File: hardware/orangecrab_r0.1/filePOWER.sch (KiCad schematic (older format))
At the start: 48 parts, among them J5 JST, U1 FAN53541, U10 NCP115-2.5, U2 FAN53541, U5 BQ24232, U7 FAN53541, U8 TPS51206

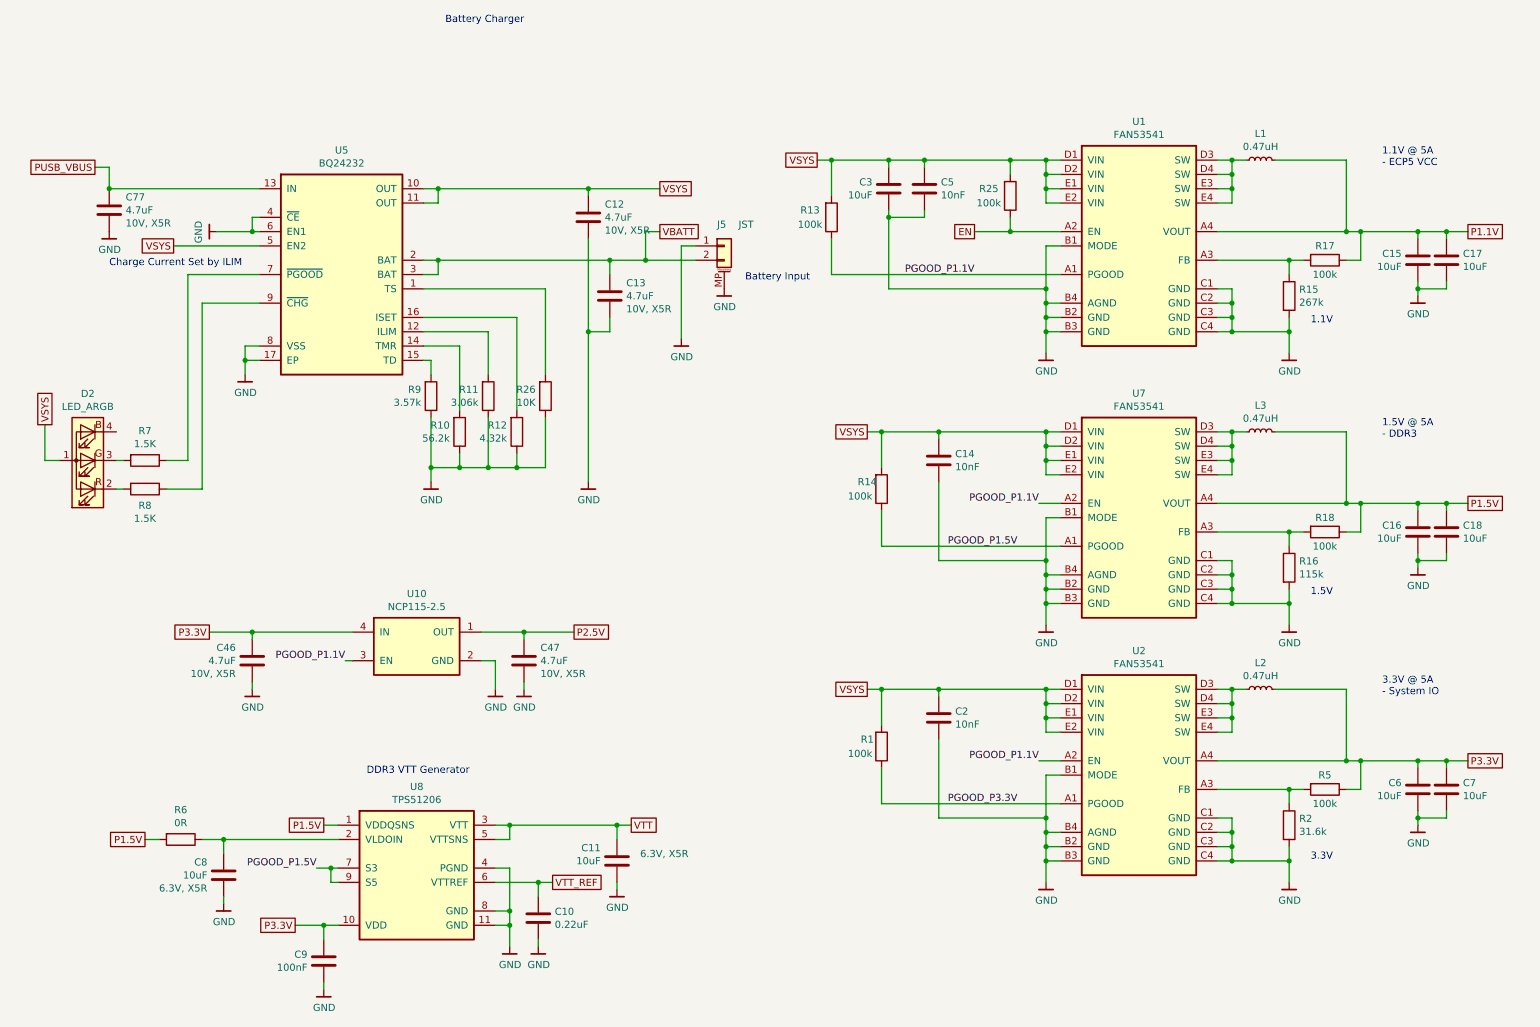
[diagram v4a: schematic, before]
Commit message: r0.1 PCB: Switch P1.5 to P1.35V
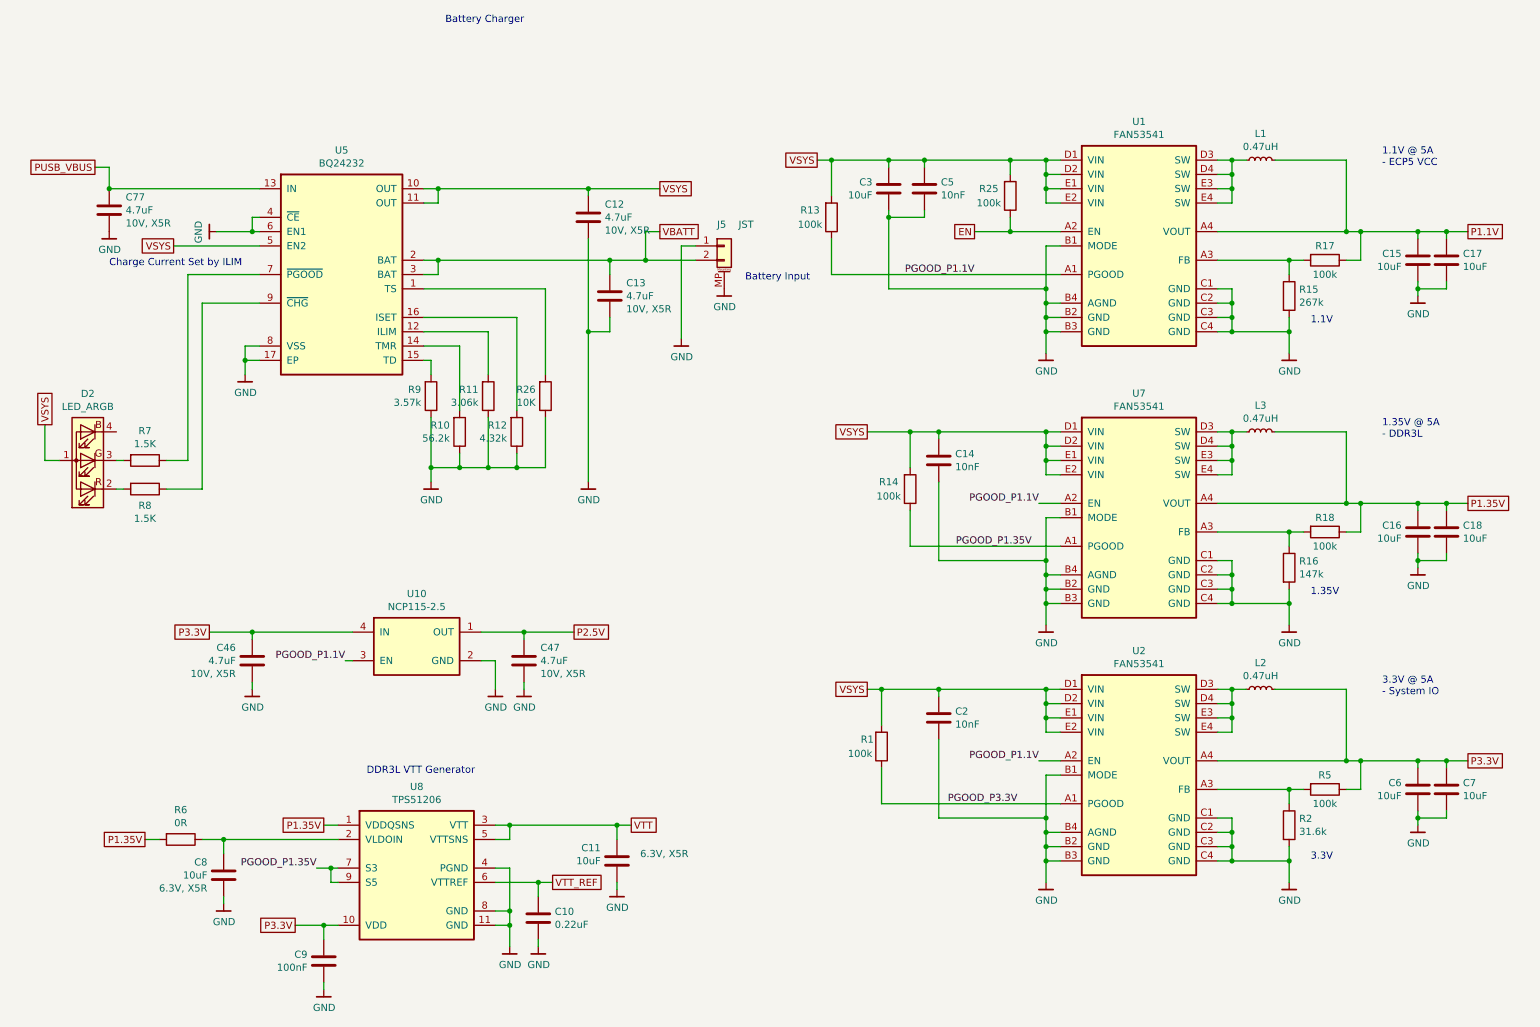
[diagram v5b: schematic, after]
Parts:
- R16: value 115k -> 147k
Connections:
- net P1.5V renamed P1.35V
- net PGOOD_P1.5V renamed PGOOD_P1.35V
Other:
- note added: "1.35V"
- note added: "1.35V @ 5A\n- DDR3L"
- note added: "DDR3L VTT Generator"
- note removed: "1.5V"
- note removed: "1.5V @ 5A\n- DDR3\n"
- note removed: "DDR3 VTT Generator"
- moved on the sheet: R14
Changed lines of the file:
@@
 EESchema Schematic File Version 4
 LIBS:OrangeCrab-cache
-EELAYER 29 0
+EELAYER 30 0
 EELAYER END
 $Descr A4 11693 8268
@@
 Connection ~ 7000 4900
 Text GLabel 10700 3600 2    50   UnSpc ~ 0
-P1.5V
+P1.35V
 $Comp
 L Device:C C12
@@
 P 9450 4050
 F 0 "R16" H 9520 4096 50  0000 L CNN
-F 1 "115k" H 9520 4005 50  0000 L CNN
+F 1 "147k" H 9520 4005 50  0000 L CNN
 F 2 "Resistor_SMD:R_0201_0603Metric" V 9380 4050 50  0001 C CNN
 F 3 "~" H 9450 4050 50  0001 C CNN
@@
 $EndComp
 Text Notes 10100 3150 0    50   ~ 0
-1.5V @ 5A\n- DDR3\n
+1.35V @ 5A\n- DDR3L
 Wire Wire Line
 	7850 3400 7750 3400
@@
 Connection ~ 7750 4100
 Wire Wire Line
-	7850 3900 6600 3900
-Wire Wire Line
-	6600 3900 6600 3650
+	7850 3900 6800 3900
+Wire Wire Line
+	6800 3900 6800 3650
 $Comp
 L Device:R R14
 U 1 1 5D3D690A
-P 6600 3500
-F 0 "R14" H 6500 3450 50  0000 C CNN
-F 1 "100k" H 6450 3550 50  0000 C CNN
-F 2 "Resistor_SMD:R_0201_0603Metric" V 6530 3500 50  0001 C CNN
-F 3 "~" H 6600 3500 50  0001 C CNN
-F 4 "‎Yageo‎" H 6600 3500 50  0001 C CNN "Mfg"
-F 5 "RC0201FR-07100KL" H 6600 3500 50  0001 C CNN "PN"
-	1    6600 3500
+P 6800 3500
+F 0 "R14" H 6650 3450 50  0000 C CNN
+F 1 "100k" H 6650 3550 50  0000 C CNN
+F 2 "Resistor_SMD:R_0201_0603Metric" V 6730 3500 50  0001 C CNN
+F 3 "~" H 6800 3500 50  0001 C CNN
+F 4 "‎Yageo‎" H 6800 3500 50  0001 C CNN "Mfg"
+F 5 "RC0201FR-07100KL" H 6800 3500 50  0001 C CNN "PN"
+	1    6800 3500
 	1    0    0    1
 $EndComp
 Wire Wire Line
-	6600 3350 6600 3100
-Connection ~ 6600 3100
-Wire Wire Line
-	6600 3100 6500 3100
+	6800 3350 6800 3100
+Connection ~ 6800 3100
+Wire Wire Line
+	6800 3100 6500 3100
 $Comp
 L gkl_power:GND #PWR0105
@@
 VSYS
 Wire Wire Line
-	6600 3100 7000 3100
+	6800 3100 7000 3100
 Wire Wire Line
 	6600 4900 7000 4900
@@
 $EndComp
 Text GLabel 1450 5950 0    50   UnSpc ~ 0
-P1.5V
+P1.35V
 Wire Wire Line
 	1550 5950 1450 5950
@@
 	2700 5850 2800 5850
 Text GLabel 2700 5850 0    50   UnSpc ~ 0
-P1.5V
+P1.35V
 Text Notes 3000 5500 0    50   ~ 0
-DDR3 VTT Generator
+DDR3L VTT Generator
 $Comp
 L gkl_pmic:TPS51206 U?
@@
 Wire Wire Line
 	2200 4500 2900 4500
-Text Label 7550 3900 2    50   ~ 0
-PGOOD_P1.5V
+Text Label 7650 3900 2    50   ~ 0
+PGOOD_P1.35V
 Text Label 7550 5700 2    50   ~ 0
 PGOOD_P3.3V
 Text Label 2650 6150 2    50   ~ 0
-PGOOD_P1.5V
+PGOOD_P1.35V
 Text GLabel 7250 1700 0    50   UnSpc ~ 0
 EN
@@
 1.1V
 Text Notes 9600 4250 0    50   ~ 0
-1.5V
+1.35V
 Text Notes 9600 6100 0    50   ~ 0
 3.3V

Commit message: hw r0.1: Update Part numbers, regenerate csv/ibom. Upload schematic
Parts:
- R16: PN RC0201FR-07115KL -> RC0201FR-07147KL
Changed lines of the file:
@@
 EESchema Schematic File Version 4
-LIBS:OrangeCrab-cache
 EELAYER 30 0
 EELAYER END
@@
 F 3 "~" H 9450 4050 50  0001 C CNN
 F 4 "‎Yageo‎" H 9450 4050 50  0001 C CNN "Mfg"
-F 5 "RC0201FR-07115KL" H 9450 4050 50  0001 C CNN "PN"
+F 5 "RC0201FR-07147KL" H 9450 4050 50  0001 C CNN "PN"
 	1    9450 4050
 	1    0    0    -1
